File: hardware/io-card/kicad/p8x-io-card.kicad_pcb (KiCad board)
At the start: 4 copper layers, 400 x 100 mm, 56 parts, among them J1 MABC96R, J2 1x3, J3 1x3, SW1 INPUT, U1 74HCT30, U10 74HCT374, U11 74HCT244, U12 74HCT244, U13 74HCT244, U14 6850, U15 74HCT00, U16 DS1302, U2 74HCT138, U3 74HCT138, U4 74HCT138, U5 74HCT32, U6 74HCT08, U7 74HCT161, U8 MAX232, U9 74HCT244, X2 2.4576MHZ, X3 32.768KHZ

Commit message: feat(kicad): re-route led/cf/control/io/alu at uniform 280x140mm
All cards rebuilt at the uniform 280x140 size with the unified courtyard-spaced
placement (0 hard DRC violations) and re-routed with Freerouting.

Co-Authored-By: Claude Opus 4.8 <noreply@anthropic.com>
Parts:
- moved RP1 324.5 mm to (58.5, 99.5)
- moved LED3 312.2 mm to (94.1, 101.3), turned to 0 degrees
- moved R4 304.1 mm to (75.8, 99.5)
- moved LED4 297.4 mm to (105.6, 101.3), turned to 0 degrees
- moved BT1 296.2 mm to (42.2, 105.1)
- moved SW1 272.7 mm to (116.5, 100.7)
- moved J2 256.7 mm to (132.3, 99.8)
- moved J3 246.1 mm to (140.9, 99.8)
- moved C15 212.7 mm to (42.5, 29.4)
- moved U10 212.7 mm to (33.6, 41.5)
- moved C16 210.6 mm to (73.5, 29.4)
- moved U11 210.6 mm to (64.6, 41.5)
- moved C17 208.5 mm to (104.5, 29.4)
- moved U12 208.5 mm to (95.5, 41.5)
- moved C18 206.3 mm to (135.5, 29.4)
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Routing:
- net RTCX1: track 249.3 -> 35.2 mm
- net RTCX2: track 248.1 -> 34.5 mm
- net A7: track 298.8 -> 90.3 mm
- net A4: track 318.8 -> 114.4 mm
- net A13: track 340.3 -> 142.7 mm, vias 2 -> 0
- net A2: track 310.9 -> 115.7 mm
- net A6: track 304.7 -> 110.5 mm
- net RTCSCLK: track 310.4 -> 123.7 mm, vias 1 -> 0
- net A10: track 331.8 -> 146.4 mm, vias 0 -> 2
- net A12: track 333.2 -> 148.7 mm, vias 1 -> 0
- net A5: track 309.5 -> 126.5 mm
- net A3: track 309.0 -> 128.6 mm
- net A1: track 308.3 -> 128.0 mm
- net A15: track 316.1 -> 135.9 mm
- net A14: track 323.8 -> 144.1 mm, vias 0 -> 1
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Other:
- board size 400 x 100 mm -> 280 x 140 mm

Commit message: feat(kicad): re-route led/cf/control/io with right-edge LED banks
Status LEDs now on the edge opposite the connector; re-routed at 280x140.
0 unconnected on all four.

Co-Authored-By: Claude Opus 4.8 <noreply@anthropic.com>
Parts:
- moved RP1 210.9 mm to (250.9, 13.3)
- moved C14 200.6 mm to (42.5, 29.4)
- moved U9 200.6 mm to (33.6, 41.5)
- moved LED3 198.7 mm to (272.3, 13.3), turned to 180 degrees
- moved R4 190.8 mm to (250.9, 23.8)
- moved LA1 185.3 mm to (49.3, 62.0)
- moved U16 185.3 mm to (33.6, 68.0)
- moved C21 185.3 mm to (34.9, 55.9)
- moved LED4 183.8 mm to (272.3, 23.8), turned to 180 degrees
- moved C2 173.0 mm to (33.1, 99.5)
- moved C3 173.0 mm to (45.3, 99.5)
- moved C4 173.0 mm to (57.5, 99.5)
- moved X3 173.0 mm to (81.9, 100.0)
- moved C5 173.0 mm to (69.7, 99.5)
- moved BT1 57.8 mm to (100.0, 105.1)
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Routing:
- net C1MN: track 35.4 -> 247.5 mm, vias 0 -> 4
- net C2MN: track 34.7 -> 245.0 mm, vias 0 -> 3
- net C1PN: track 37.9 -> 239.9 mm, vias 0 -> 4
- net C2PN: track 33.1 -> 234.7 mm, vias 0 -> 2
- net VPN: track 62.5 -> 250.5 mm, vias 2 -> 3
- net VMN: track 45.0 -> 195.5 mm, vias 1 -> 3
- net VBAT: track 235.6 -> 106.4 mm, vias 1 -> 2
- net D4: track 320.0 -> 240.9 mm
- net A2: track 115.7 -> 192.7 mm, vias 1 -> 2
- net LR2: track 94.3 -> 161.5 mm, vias 2 -> 0
- net LR0: track 97.1 -> 162.7 mm, vias 2 -> 0
- net A4: track 114.4 -> 176.1 mm
- net LR1: track 99.7 -> 161.1 mm
- net SELP: track 151.9 -> 91.3 mm, vias 2 -> 0
- net A6: track 110.5 -> 170.7 mm, vias 1 -> 3
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
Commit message: build: re-route all boards via the build+verify flow (keepouts + stitch)
Ran build.sh all + build.sh backplane. Every board regenerated + re-routed fresh
with the mounting-hole keepouts, the self-heal stitch, and -mt 1. Final verdicts:
  PASS (clean): cf, control, alu, regbank, memory
  1 unconnected net (non-collinear, stitch gap): io, peripheral
  18 unconnected (dense ~960-pin bus, router cap): backplane
  3 blocking DRC: bustest
All boards now PASS the DIN mounting-hole keepout check; 0 blocking DRC except
bustest. Gerbers/renders/placement + DRC reports regenerated per card.

Co-Authored-By: Claude Opus 4.8 <noreply@anthropic.com>
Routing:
- net ML2_2: track 106.2 -> 170.7 mm, vias 0 -> 2
- net A1: track 151.9 -> 201.6 mm, vias 0 -> 1
- net SIN: track 206.7 -> 159.8 mm, vias 2 -> 0
- net VPN: track 250.5 -> 205.1 mm, vias 3 -> 4
- net ML1_3: track 163.9 -> 128.4 mm, vias 3 -> 1
- net MA13: track 105.6 -> 138.9 mm, vias 0 -> 3
- net MA5: track 160.8 -> 129.0 mm, vias 2 -> 1
- net ML0_1: track 143.6 -> 173.6 mm, vias 0 -> 5
- net ML2_4: track 111.8 -> 140.3 mm
- net ML2_1: track 135.0 -> 107.3 mm, vias 1 -> 0
- net DLD2: track 144.2 -> 169.6 mm, vias 2 -> 1
- net A6: track 170.7 -> 145.9 mm, vias 3 -> 2
- net C1MN: track 247.5 -> 227.0 mm, vias 4 -> 3
- net DOE1: track 139.6 -> 120.5 mm, vias 2 -> 0
- net ML2_3: track 104.6 -> 122.0 mm, vias 0 -> 5
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
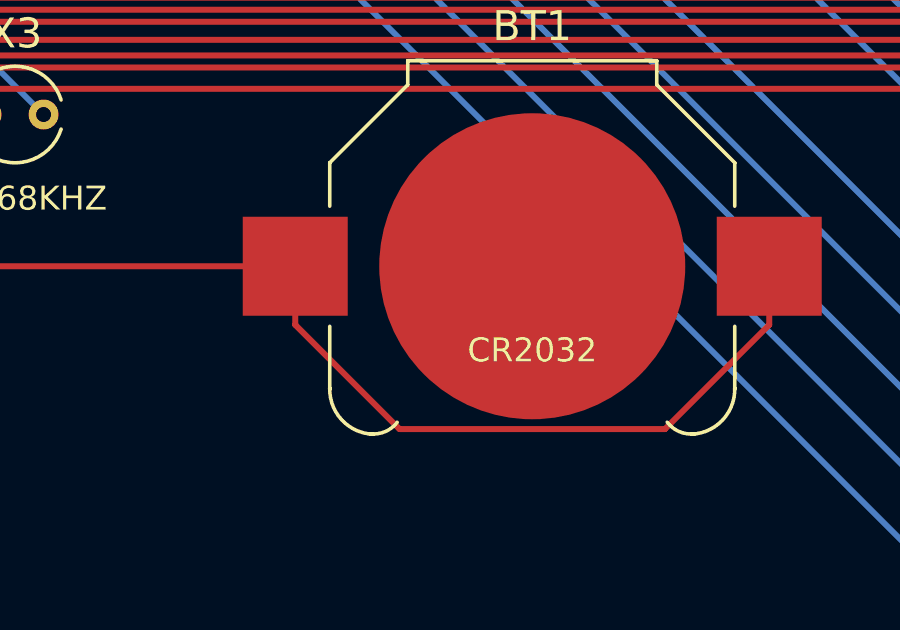
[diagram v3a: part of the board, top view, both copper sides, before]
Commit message: fix(kicad): heal plane-net orphans + edge-hugging tracks; io/peripheral/bustest PASS
Add two deterministic post-route heal passes to the shared pipeline
(generators/kicad_tools.py), wired into import_ses so every card gets them:

* heal_unconnected(): the realistic leftover on these boards is a plane-net
  orphan -- an SMD pad on GND/VCC that can't reach the In1/In2 plane through a
  barrel and whose F.Cu tie the router skipped. The DNP Keystone coin-cell
  holder BT1 is exactly this (surface-mount GND pad). The plane copper is solid
  a couple mm away, so it drops a stitching VIA into solid same-net plane + a
  short F.Cu track, choosing a site clear of other pads AND foreign tracks. It
  only heals when a clean site exists; a non-plane miss is left for a human
  rather than risking a blind cross-board track.

* heal_edge_clearance(): pulls any track vertex that sits inside the 0.5mm
  copper-to-edge rule back in, measured to the Edge.Cuts centreline (the board
  bbox includes the cut line's half-width, which is what made the first attempt
  miss by exactly 0.075mm).

* export_dsn now insets the Freerouting routing boundary by 0.35mm so the router
  keeps copper off the board edge from the start -- the bustest A2 bus tracks
  were hugging the DIN edge at 0.468mm and no post-nudge could re-space them in
  that congested corner. A fresh route with the inset clears it.

Result: io-card, peripheral-card and bustest-card all PASS the full readiness
check (0 blocking DRC, 0 unconnected, keepout + fab clean). Boards + gerbers +
renders regenerated. GENERATORS ARE CANON.

Co-Authored-By: Claude Opus 4.8 <noreply@anthropic.com>
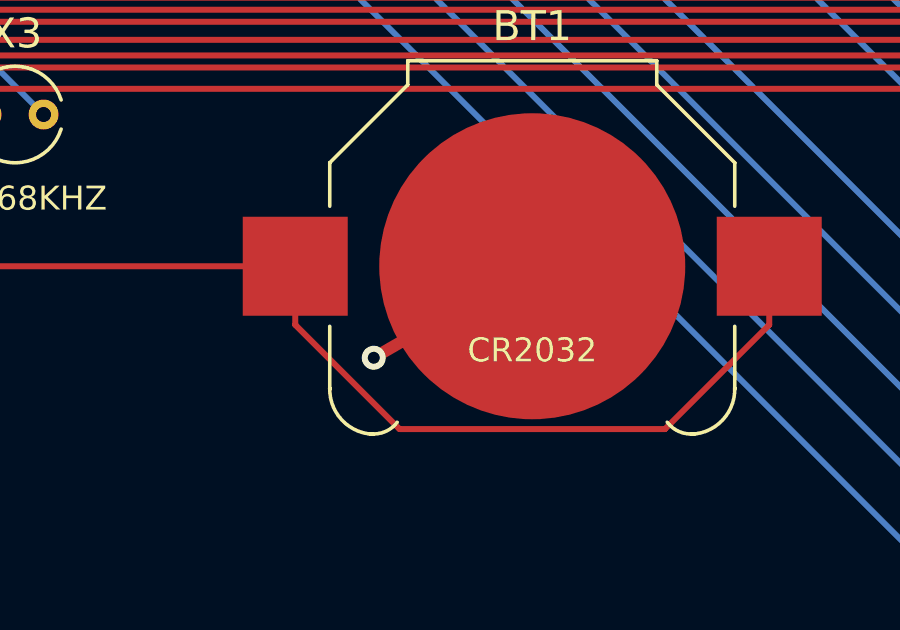
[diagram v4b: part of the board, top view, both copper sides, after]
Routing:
- net GND: track 0.00 -> 6.10 mm, vias 0 -> 1
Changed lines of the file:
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@@
+	)
+	(segment
+		(start 100.0425 105.1)
+		(end 94.759745 108.149999)
+		(width 0.4)
+		(layer "F.Cu")
+		(net "GND")
+	)
+	(via
+		(at 94.759745 108.149999)
+		(size 0.8)
+		(drill 0.4)
+		(layers "F.Cu" "B.Cu")
+		(net "GND")
 	)
 	(segment

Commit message: feat(io,cf): io rev B (2x ACIA/DB9) + cf rev B (2 CF drives), both PASS
Per the user's direction, the two standalone cards get their upgrades + edge
treatment. Both route clean (ERC 0 errors, 0 unconnected, 0 blocking DRC).

io-card rev B -- serial upgrades:
* 2nd ACIA (U17 6850) at $FF08/09 (already in the memory map), on MAX232 channel 2;
  one MAX232 serves both channels. Both serial ports go through a RX/TX swap jumper
  (JP1/JP2, straight or null-modem) to a DB9 socket (DB9A/DB9B). U18 HEX inverter
  provides ACIA2's E-gate (P4P). $FF08 was the RTC's old reserved slot -- the RTC
  (DS1302/coin cell) is a bit-banged 3-wire DNP peripheral on J3, not memory-mapped.
* Bespoke placement (gen_io.py): DB9 sockets + DIP switch + RTC header on the bottom
  edge, the four LED bars on the top edge, bus DIN on the left; the swap jumpers flow
  in the interior (set-once config -- crowding them beside the big edge-mount DB9s
  left the DB9 TXD/RXD pins unroutable).

cf-card rev B -- two 8-bit True IDE drives (no fragile master/slave):
* drive 0 command block $FF10-17 (J2, now command-only), drive 1 command block
  $FF18-1F on its own header J5. Each drive has its own 74245 data buffer (U1/U10),
  strobe glue (U11 + the freed U8/U5 gates), pull-up network (RN1/RN3), and activity
  LED (LED4/LED6). Two CF-IDE adapters plug in as independent masters.
* Bespoke placement (gen_cf.py): the two IDE-40 headers 71mm apart on the right so
  the two adapter bodies (~43x50mm each) don't collide; bus DIN left, LEDs far-right.
* SOFTWARE STILL NEEDED for drive 1: the firmware CF driver uses fixed $FF10-17
  addresses throughout, so drive 1 needs a drive-selectable port base in
  CFSETL/CFINIT + the emulator's port decode (data-integrity-critical -> separate,
  test-validated change). DRIVE 0 WORKS UNCHANGED on the current firmware.

Both cards wired into build.sh. GENERATORS ARE CANON.

Co-Authored-By: Claude Opus 4.8 <noreply@anthropic.com>
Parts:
- removed J2: 1x3, PinHeader_1x03_P2.54mm_Vertical
- added C22: 100nF, C_Disc_D5.0mm_W2.5mm_P5.00mm, F.Cu at (179.0, 52.4)
- added C23: 100nF, C_Disc_D5.0mm_W2.5mm_P5.00mm, F.Cu at (205.5, 52.4)
- added DB9A: SERIAL1, DSUB-9_Socket_Horizontal_P2.77x2.54mm_EdgePinOffset9.40mm, F.Cu at (34.5, 127.3)
- added DB9B: SERIAL2, DSUB-9_Socket_Horizontal_P2.77x2.54mm_EdgePinOffset9.40mm, F.Cu at (89.5, 127.3)
- added JP1: S1 SWAP, PinHeader_2x03_P2.54mm_Vertical, F.Cu at (193.0, 79.9)
- added JP2: S2 SWAP, PinHeader_2x03_P2.54mm_Vertical, F.Cu at (203.5, 79.9)
- added U17: 6850, DIP-24_W15.24mm, F.Cu at (167.5, 71.0)
- added U18: 74HCT14, DIP-14_W7.62mm, F.Cu at (200.4, 63.3)
- moved RL1 190.6 mm to (18.8, 77.3), turned to 90 degrees
- moved C2 181.6 mm to (213.8, 81.6), turned to 90 degrees
- moved C3 174.3 mm to (218.7, 81.6), turned to 90 degrees
- moved C4 167.0 mm to (223.5, 81.6), turned to 90 degrees
- moved C5 159.8 mm to (228.4, 81.6), turned to 90 degrees
- moved C14 159.3 mm to (201.6, 36.2)
- moved U9 159.2 mm to (192.7, 47.2)
- moved C15 156.1 mm to (229.4, 36.2)
- moved U10 156.0 mm to (220.5, 47.2)
- moved RM1 156.0 mm to (62.4, 77.3), turned to 90 degrees
- moved X3 153.5 mm to (233.8, 78.5), turned to 90 degrees
- moved BT1 146.0 mm to (244.8, 85.7), turned to 90 degrees
- moved U16 121.5 mm to (155.0, 63.3)
- moved RM2 121.5 mm to (105.9, 77.3), turned to 90 degrees
- moved C21 121.5 mm to (156.3, 52.4)
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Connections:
- U2 pad 11: (no net) -> -P4
- U6 pad 11: (no net) -> E2
- U6 pad 12: (no net) -> P4P
- U6 pad 13: (no net) -> CLKB
- U8 pad 10: (no net) -> TXD2
- U8 pad 7: (no net) -> SOUT2
- U8 pad 8: (no net) -> SIN2
- U8 pad 9: (no net) -> RXD2
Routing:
- net S1TXD: track 0.00 -> 196.0 mm, vias 0 -> 1
- net S1RXD: track 0.00 -> 194.4 mm, vias 0 -> 1
- net -P4: track 0.00 -> 191.7 mm, vias 0 -> 2
- net C2MN: track 227.8 -> 55.2 mm, vias 3 -> 0
- net C2PN: track 234.2 -> 64.0 mm, vias 3 -> 0
- net C1MN: track 227.0 -> 57.4 mm, vias 3 -> 1
- net C1PN: track 224.7 -> 66.1 mm, vias 3 -> 1
- net S2TXD: track 0.00 -> 155.6 mm, vias 0 -> 1
- net S2RXD: track 0.00 -> 148.9 mm, vias 0 -> 1
- net VMN: track 204.4 -> 64.3 mm, vias 3 -> 0
- net VPN: track 205.1 -> 68.4 mm, vias 4 -> 1
- net A1: track 201.6 -> 70.5 mm, vias 1 -> 0
- net LP1: track 141.4 -> 266.3 mm, vias 1 -> 3
- net A2: track 183.1 -> 67.2 mm, vias 3 -> 0
- net SIN: track 159.8 -> 46.5 mm
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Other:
- board text removed: "IOSEL"
- board text removed: "PWR"
- board text removed: "RTC 3-WIRE"
- board text removed: "SERIAL"
